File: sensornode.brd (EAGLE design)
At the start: 113 x 61 mm, 72 parts, among them IC1 CP2104, Q1 mmbt2222, Q2 mmbt2222, Q3 DMG3415U, SW2 KMR2, U1 TSL2591, U2 AP2112-3.3, U3 MCP73831T-2ACI/OT, U4 BMEx80, X2 ESP32_WROOM32_SKINNY, X4 20329

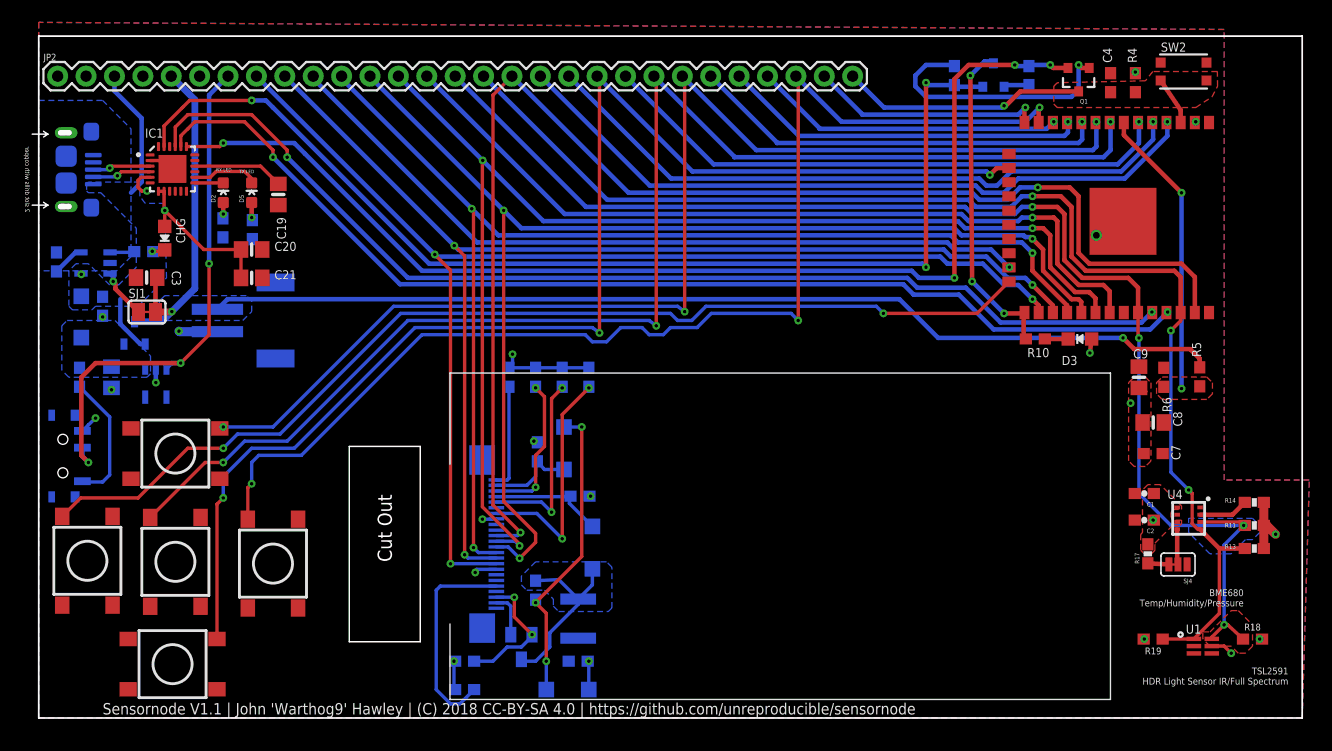
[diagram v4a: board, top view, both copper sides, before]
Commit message: Adjusting board width
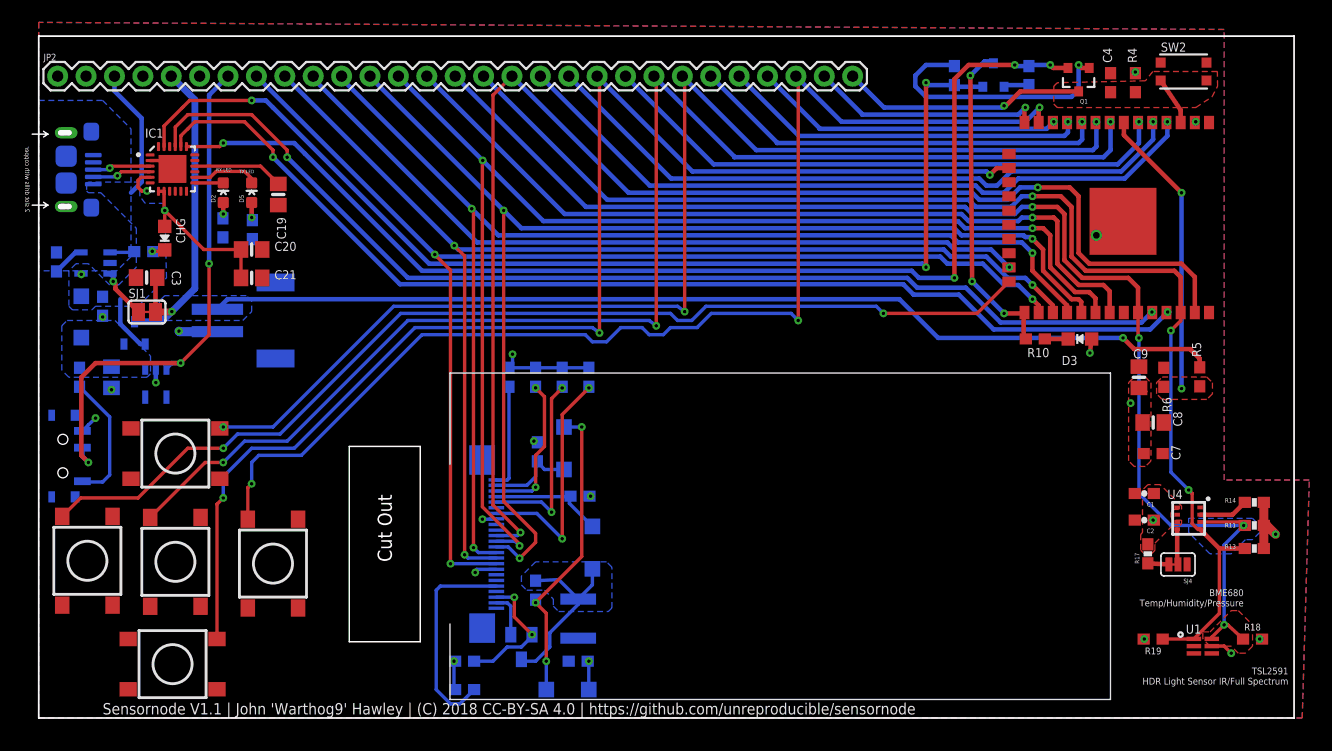
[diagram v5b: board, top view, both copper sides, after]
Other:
- board size 113 x 61 mm -> 112.3 x 61 mm
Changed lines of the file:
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@@
 <board>
 <plain>
-<wire x1="113.03" y1="0" x2="113.03" y2="61" width="0.1524" layer="20"/>
-<wire x1="113.03" y1="61" x2="0" y2="61" width="0.1524" layer="20"/>
+<wire x1="112.3" y1="0" x2="112.3" y2="61" width="0.1524" layer="20"/>
+<wire x1="112.3" y1="61" x2="0" y2="61" width="0.1524" layer="20"/>
 <wire x1="0" y1="61" x2="0" y2="0" width="0.1524" layer="20"/>
-<wire x1="0" y1="0" x2="113.03" y2="0" width="0.1524" layer="20"/>
+<wire x1="0" y1="0" x2="112.3" y2="0" width="0.1524" layer="20"/>
 <text x="17.93875" y="48.73625" size="0.3048" layer="21">TX LED</text>
 <text x="15.875" y="48.895" size="0.3048" layer="21">RX LED</text>

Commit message: Getting the updates in
Yes, this is a terrible commit
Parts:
- C19: value 10uF -> 4.7uF
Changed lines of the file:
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@@
 </element>
 <element name="U1" library="microbuilder" package="DFN6_TAOS" value="TSL2591" x="104.14" y="6.43"/>
-<element name="C19" library="microbuilder" package="0805-NO" value="10uF" x="21.43125" y="46.83125" rot="R270"/>
+<element name="C19" library="microbuilder" package="0805-NO" value="4.7uF" x="21.43125" y="46.83125" rot="R270"/>
 <element name="C20" library="microbuilder" package="0805-NO" value="10uF" x="19.05" y="41.91"/>
 <element name="C21" library="microbuilder" package="0805-NO" value="0.1uF" x="19.05" y="39.37"/>

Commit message: Adjusting some signal names
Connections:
- net A5_IO4 renamed EINK_BUSY_A5_IO4
- net GDR renamed EINK_GDR
- net IO16 renamed EINK_RESET_IO16
- net IO17 renamed EINK_DC_IO17
- net IO23 renamed EINK_MOSI_IO23
- net MOSI renamed EINK_SCLK_MOSI
- net RESE renamed EINK_RESE
- net SCK renamed EINK_CS_SCK
- net VGH renamed EINK_VGH
- net VGL renamed EINK_VGL
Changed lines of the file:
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@@
 <wire x1="68.00125" y1="52.07" x2="62.655" y2="57.41625" width="0.4064" layer="16"/>
 </signal>
-<signal name="IO16">
+<signal name="EINK_RESET_IO16">
 <contactref element="X2" pad="27"/>
 <wire x1="90.725" y1="36.2675" x2="90.725" y2="36.91" width="0.4064" layer="1"/>
@@
 <via x="37.175625" y="42.255625" extent="1-16" drill="0.3048"/>
 </signal>
-<signal name="IO17">
+<signal name="EINK_DC_IO17">
 <contactref element="X2" pad="28"/>
 <wire x1="91.995" y1="36.2675" x2="91.995" y2="36.91" width="0.4064" layer="1"/>
@@
 <via x="38.735" y="45.56125" extent="1-16" drill="0.3048"/>
 </signal>
-<signal name="MOSI">
+<signal name="EINK_SCLK_MOSI">
 <contactref element="X2" pad="30"/>
 <wire x1="94.535" y1="36.2675" x2="94.535" y2="37.545" width="0.4064" layer="1"/>
@@
 <via x="39.715625" y="49.875625" extent="1-16" drill="0.3048"/>
 </signal>
-<signal name="A5_IO4">
+<signal name="EINK_BUSY_A5_IO4">
 <contactref element="X2" pad="26"/>
 <wire x1="89.455" y1="36.2675" x2="89.455" y2="36.91" width="0.4064" layer="1"/>
@@
 <wire x1="36.83635" y1="40.0549" x2="36.83635" y2="13.8049" width="0.3048" layer="1"/>
 </signal>
-<signal name="IO23">
+<signal name="EINK_MOSI_IO23">
 <contactref element="X2" pad="37"/>
 <wire x1="103.425" y1="36.2675" x2="103.425" y2="39.45" width="0.4064" layer="1"/>
@@
 <wire x1="47.04625" y1="45.085" x2="34.715" y2="57.41625" width="0.4064" layer="16"/>
 </signal>
-<signal name="SCK">
+<signal name="EINK_CS_SCK">
 <contactref element="X2" pad="29"/>
 <wire x1="93.265" y1="36.2675" x2="93.265" y2="37.2275" width="0.4064" layer="1"/>
@@
 <wire x1="101.1047" y1="13.7325" x2="99.21875" y2="13.835" width="0.4064" layer="1"/>
 </signal>
-<signal name="VGL">
+<signal name="EINK_VGL">
 <contactref element="C11" pad="2"/>
 <contactref element="D1" pad="A"/>
@@
 <wire x1="45.4075" y1="5.075" x2="45.4025" y2="5.08" width="0.3048" layer="16"/>
 </signal>
-<signal name="VGH">
+<signal name="EINK_VGH">
 <contactref element="D7" pad="C"/>
 <contactref element="C10" pad="2"/>
@@
 <wire x1="47.46875" y1="19.20125" x2="49.53" y2="17.14" width="0.3048" layer="16"/>
 </signal>
-<signal name="GDR">
+<signal name="EINK_GDR">
 <contactref element="Q4" pad="1"/>
 <contactref element="U$15" pad="2-GDR"/>
@@
 <wire x1="42.2275" y1="7.4525" x2="42.23" y2="7.45" width="0.3048" layer="16"/>
 </signal>
-<signal name="RESE">
+<signal name="EINK_RESE">
 <contactref element="Q4" pad="2"/>
 <contactref element="R16" pad="1"/>

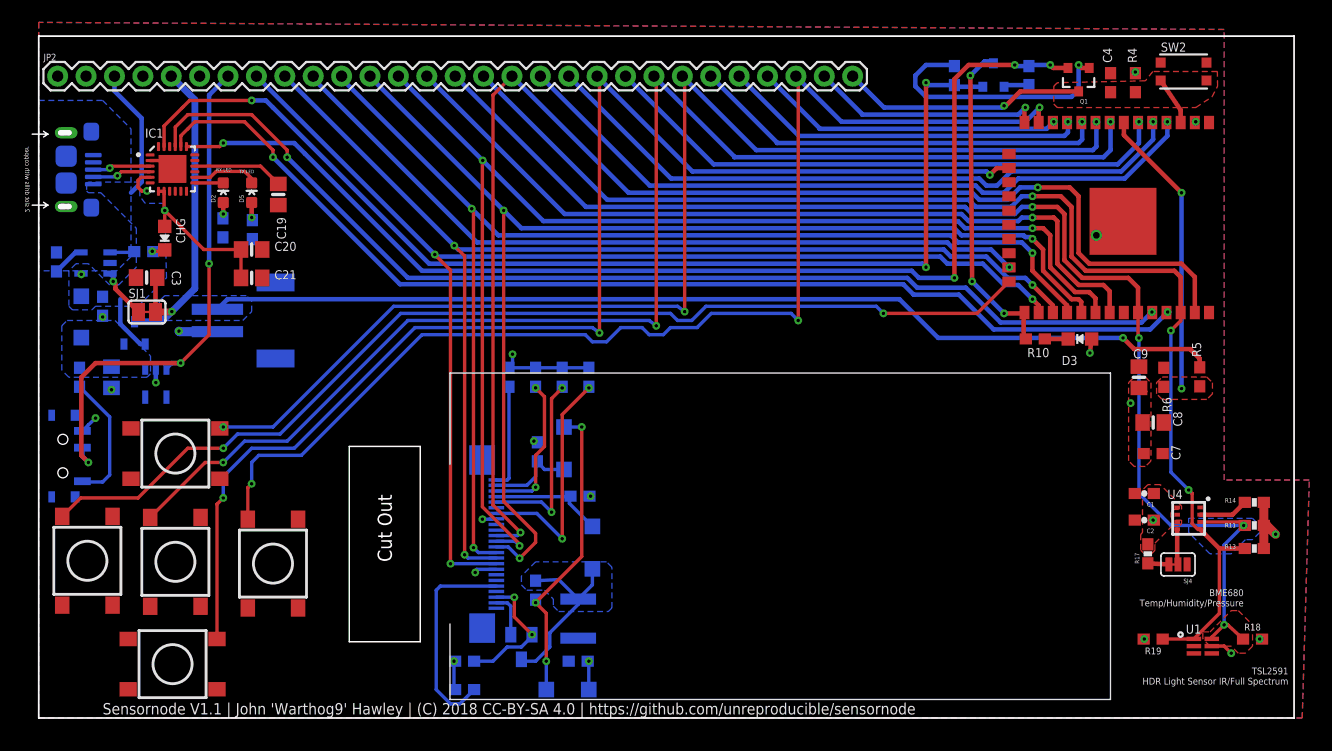
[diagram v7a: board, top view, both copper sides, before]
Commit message: Adding SD Card
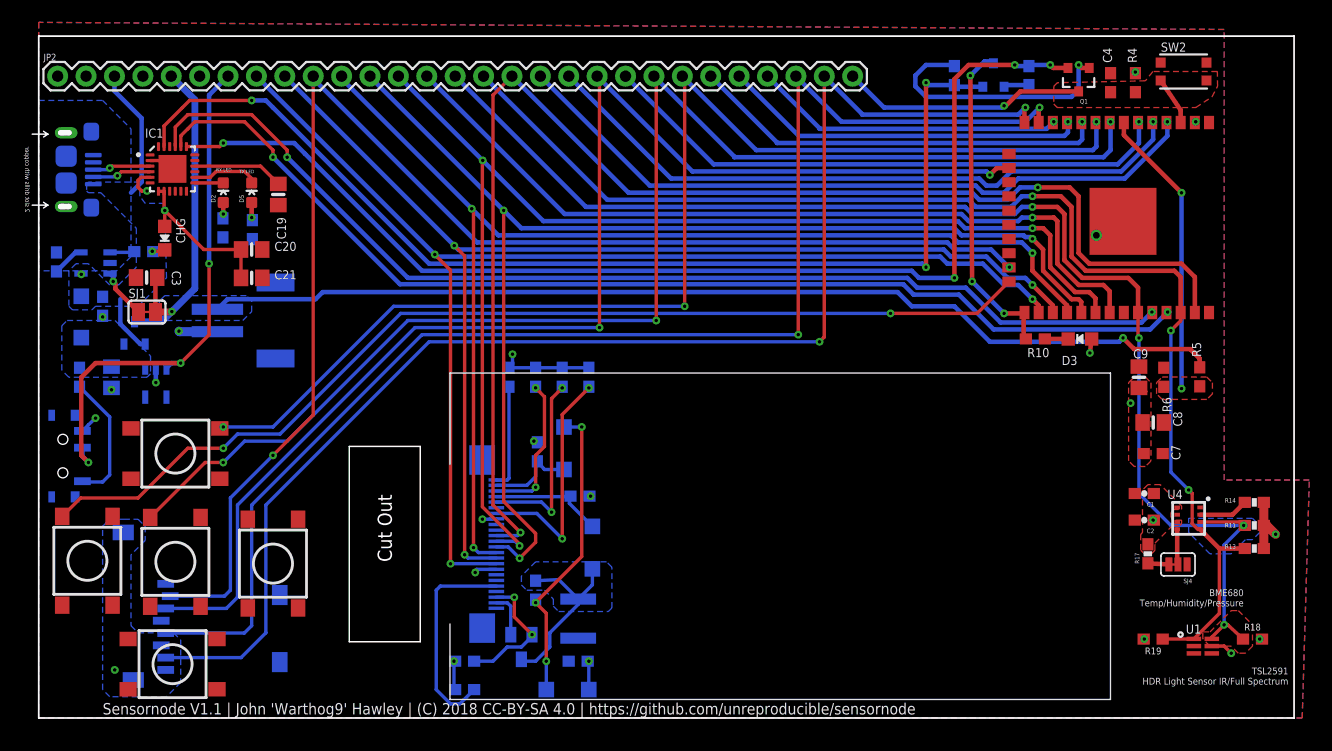
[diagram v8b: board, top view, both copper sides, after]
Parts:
- added U$17: MICROSD, adafruit:MICROSD
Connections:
- removed net IO12_A11: JP2.28, X2.14
- removed net IO13_A12: JP2.20, S2.B2, X2.16
- removed net IO14_A6: JP2.27, S4.B2, X2.13
- removed net IO15_A8: JP2.10, X2.23
- new net HSPI_CS0-IO15_A8: JP2.10, U$17.2, X2.23
- new net HSPI_MISO-IO12_A11: JP2.28, U$17.7, X2.14
- new net HSPI_MOSI-IO13_A12: JP2.20, U$17.3, X2.16
- new net HSPI_SCLK-IO14_A6: JP2.27, U$17.5, X2.13
- new net N$21: S2.B2
- new net N$6: S4.B2
- net 3.3V: now also U$17.4
- net GND: now also U$17.6, U$17.MT1, U$17.MT2
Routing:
- net HSPI_CS0-IO15_A8: track 0.00 -> 124.3 mm, vias 0 -> 2
- net HSPI_SCLK-IO14_A6: track 0.00 -> 122.6 mm, vias 0 -> 2
- net HSPI_MISO-IO12_A11: track 0.00 -> 121.9 mm, vias 0 -> 2
- net IO13_A12: track 117.9 -> 0.00 mm, vias 3 -> 0
- net HSPI_MOSI-IO13_A12: track 0.00 -> 117.4 mm, vias 0 -> 2
- net IO14_A6: track 108.3 -> 0.00 mm, vias 3 -> 0
- net IO15_A8: track 69.7 -> 0.00 mm, vias 1 -> 0
- net IO12_A11: track 21.1 -> 0.00 mm, vias 1 -> 0
- net GPIO2: track 94.4 -> 93.4 mm
- net VBAT: track 122.3 -> 123.2 mm
- net IO33_A9: track 109.7 -> 109.0 mm
- net IO32_A7: track 121.9 -> 121.3 mm
- net GND: vias 13 -> 14
